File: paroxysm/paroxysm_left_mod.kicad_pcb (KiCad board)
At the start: 2 copper layers, 117.5 x 89.9 mm, 21 parts, among them SW10 SW_Push, SW11 SW_Push, SW12 SW_Push, SW14 SW_Push, SW15 SW_Push, SW16 SW_Push, SW17 SW_Push, SW18 SW_Push, SW20 SW_Push, SW21 SW_Push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

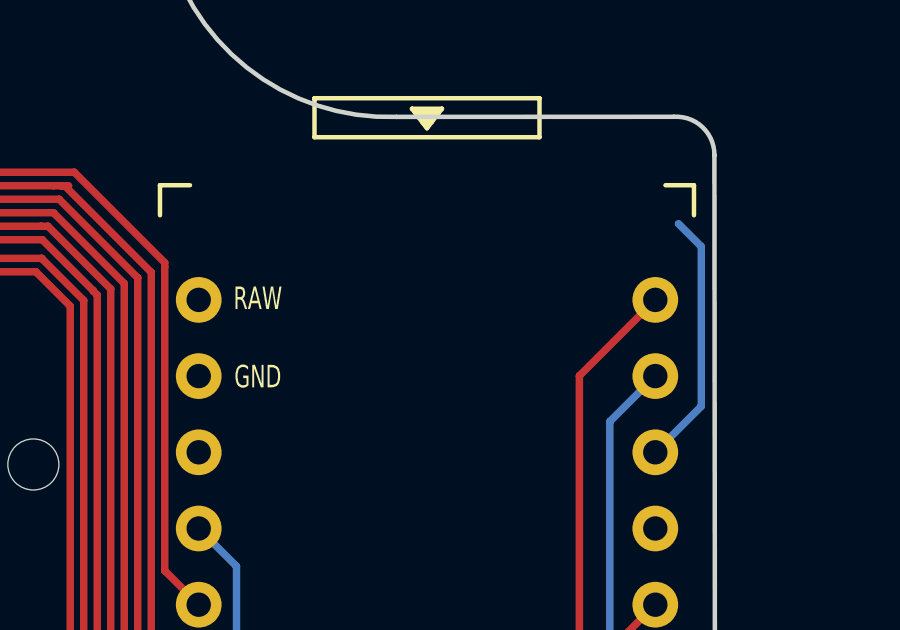
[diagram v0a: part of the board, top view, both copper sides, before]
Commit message: Update and corrected traces
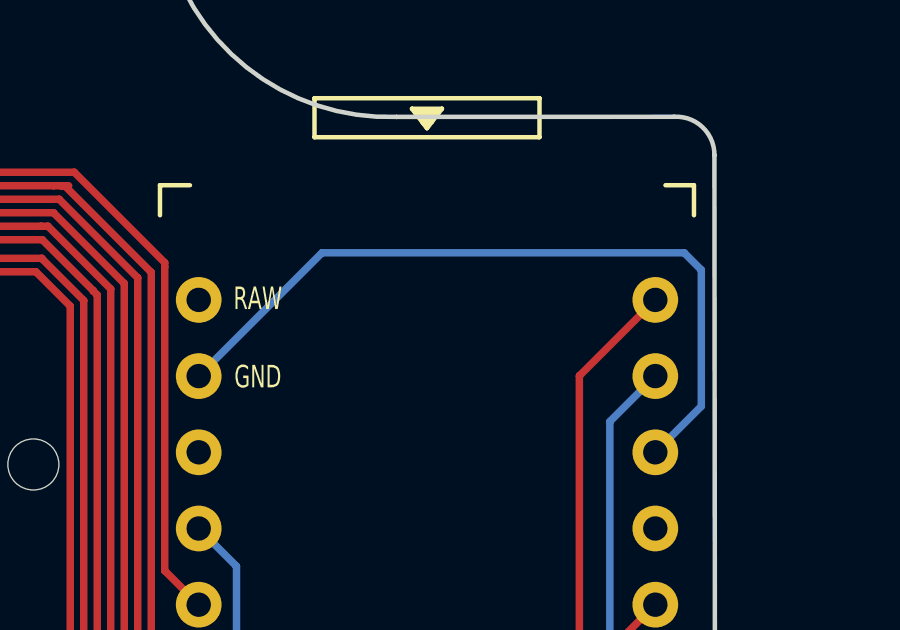
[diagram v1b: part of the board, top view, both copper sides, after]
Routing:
- net gnd: track 9.07 -> 25.9 mm
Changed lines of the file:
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@@
   (segment (start 210.0466 76.2) (end 210.54277 76.2) (width 0.25) (layer "F.Cu") (net 2))
   (segment (start 211.582 74.6674) (end 210.0494 76.2) (width 0.25) (layer "B.Cu") (net 2))
-  (segment (start 211.582 69.342) (end 211.582 74.6674) (width 0.25) (layer "B.Cu") (net 2))
-  (segment (start 210.82 68.58) (end 211.582 69.342) (width 0.25) (layer "B.Cu") (net 2))
+  (segment (start 211.582 70.118) (end 211.014 69.55) (width 0.25) (layer "B.Cu") (net 2))
+  (segment (start 211.582 74.6674) (end 211.582 70.118) (width 0.25) (layer "B.Cu") (net 2))
+  (segment (start 198.9394 69.55) (end 194.8294 73.66) (width 0.25) (layer "B.Cu") (net 2))
+  (segment (start 211.014 69.55) (end 198.9394 69.55) (width 0.25) (layer "B.Cu") (net 2))
   (segment (start 207.112 106.958) (end 207.092 106.978) (width 0.25) (layer "F.Cu") (net 3))
   (segment (start 196.088 103.886) (end 197.575001 105.373001) (width 0.25) (layer "B.Cu") (net 3))
